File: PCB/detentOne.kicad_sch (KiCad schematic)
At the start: 0 parts

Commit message: Adding microSD
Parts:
- added U3: ESP32-S3-WROOM-1(N16R8), easyeda2kicad:WIRELM-SMD_ESP32-S3-WROOM-1, symbol easyeda2kicad:ESP32-S3-WROOM-1(N16R8)
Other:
- added sheet Encoder (Encoder.kicad_sch)
- added sheet OLED (untitled.kicad_sch)
- added sheet Switches (Switches.kicad_sch)
- added sheet TMC6300 BLDC Driver (TMC6300_BLDC.kicad_sch)
- added sheet microSD (microSD.kicad_sch)

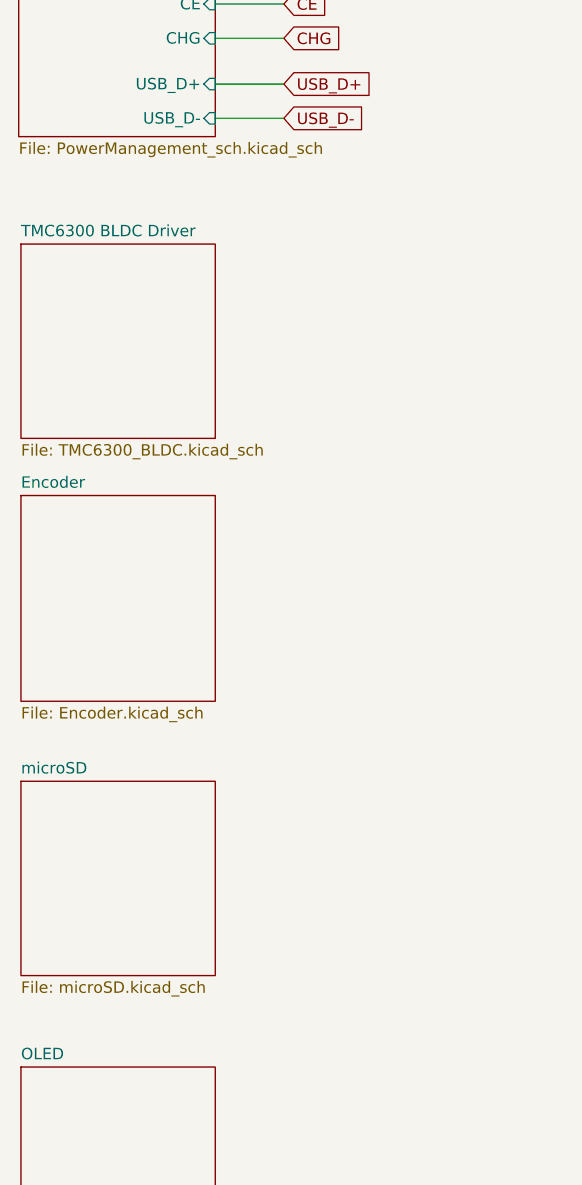
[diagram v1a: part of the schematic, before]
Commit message: Added bldc driver
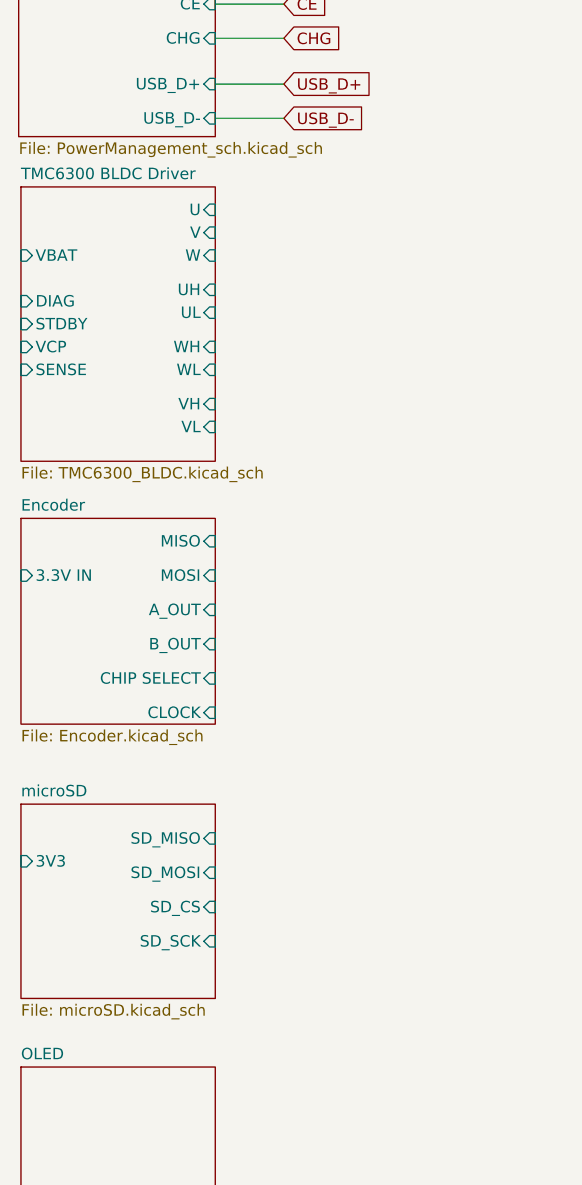
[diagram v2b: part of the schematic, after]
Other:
- sheet Encoder ports: added 3.3V IN, A_OUT, B_OUT, CHIP SELECT, CLOCK, MISO, MOSI; removed none
- sheet TMC6300 BLDC Driver ports: added DIAG, SENSE, STDBY, U, UH, UL, V, VBAT, VCP, VH, VL, W, WH, WL; removed none
- sheet microSD ports: added 3V3, SD_CS, SD_MISO, SD_MOSI, SD_SCK; removed none
- title: (none) -> detent One

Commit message: Finished schematic
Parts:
- added C16, C18: 0.1uF 6.3V, Capacitor_SMD:C_0603_1608Metric_Pad1.08x0.95mm_HandSolder, symbol Device:C
- added C17: 10uF 6.3V, Capacitor_SMD:C_0603_1608Metric_Pad1.08x0.95mm_HandSolder, symbol Device:C
- added R20, R21: 10K, Resistor_SMD:R_0603_1608Metric_Pad0.98x0.95mm_HandSolder, symbol Device:R
- added SW7, SW8: C92589, easyeda2kicad:KEY-SMD_4P-L4.2-W3.2-P2.20-LS5.1-TL, symbol Switch:SW_MEC_5E
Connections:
- net 3V3: now also U3.2 (3V3), C16.2, C17.2, R20.1, R21.2
- net CE: now also U3.39 (IO1)
- net CHG: now also U3.38 (IO2)
- net USB_D+: now also U3.14 (IO20)
- net USB_D-: now also U3.13 (IO19)
- net GND: now reaches U3.1 (GND)
- net GND: now also C16.1, C17.1, C18.2, SW7.1, SW7.2, SW8.1, SW8.2
- net A_OUT: now reaches U3.10 (IO17)
- net B_OUT: now reaches U3.11 (IO18)
- net CURRENT_SENSE: now reaches U3.12 (IO8)
- net OLED_DC: now reaches U3.17 (IO9)
- net OLED_RST: now reaches U3.18 (IO10)
- net MOSI: now reaches U3.19 (IO11)
- net SCK: now reaches U3.20 (IO12)
- net MISO: now reaches U3.21 (IO13)
- net NEOPIXEL_DIN: now reaches U3.22 (IO14)
- net ENCODER_CS: now reaches U3.23 (IO21)
- net BOOT: now reaches U3.27 (IO0)
- net BOOT: now also R21.1, SW8.3 (K), SW8.4 (A)
- net EN: now reaches U3.3 (EN)
- net EN: now also C18.1, R20.2, SW7.3 (K), SW7.4 (A)
- net SDA: now reaches U3.31 (IO38)
- net SCL: now reaches U3.32 (IO39)
- net KEY_INT: now reaches U3.33 (IO40)
- net SD_CS: now reaches U3.34 (IO41)
- net OLED_CS: now reaches U3.35 (IO42)
- net UH: now reaches U3.4 (IO4)
- net UL: now reaches U3.5 (IO5)
- net WH: now reaches U3.6 (IO6)
- net WL: now reaches U3.7 (IO7)
- net VH: now reaches U3.8 (IO15)
- net VL: now reaches U3.9 (IO16)
- no-connect marks 0 -> 10
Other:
- added sheet NeoPixels (NeoPixels.kicad_sch)
- sheet OLED ports: added 3V3, CLK, CS, DC, DIN, RST; removed none
- sheet Switches ports: added 3V3, INT, SCL, SDA; removed none
- sheet TMC6300 BLDC Driver ports: added 3V3; removed DIAG, STDBY, VCP
- note added: "BOOT BUTTON"
- note added: "RESET BUTTON & PWR ON RESET"
- moved on the sheet: U3

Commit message: PCB layout done
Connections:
- net UH: now also U3.9 (IO16); no longer U3.4 (IO4)
- net UL: now also U3.6 (IO6); no longer U3.5 (IO5)
- net VL: now also U3.4 (IO4); no longer U3.9 (IO16)
- net WH: now also U3.7 (IO7); no longer U3.6 (IO6)
- net WL: now also U3.5 (IO5); no longer U3.7 (IO7)

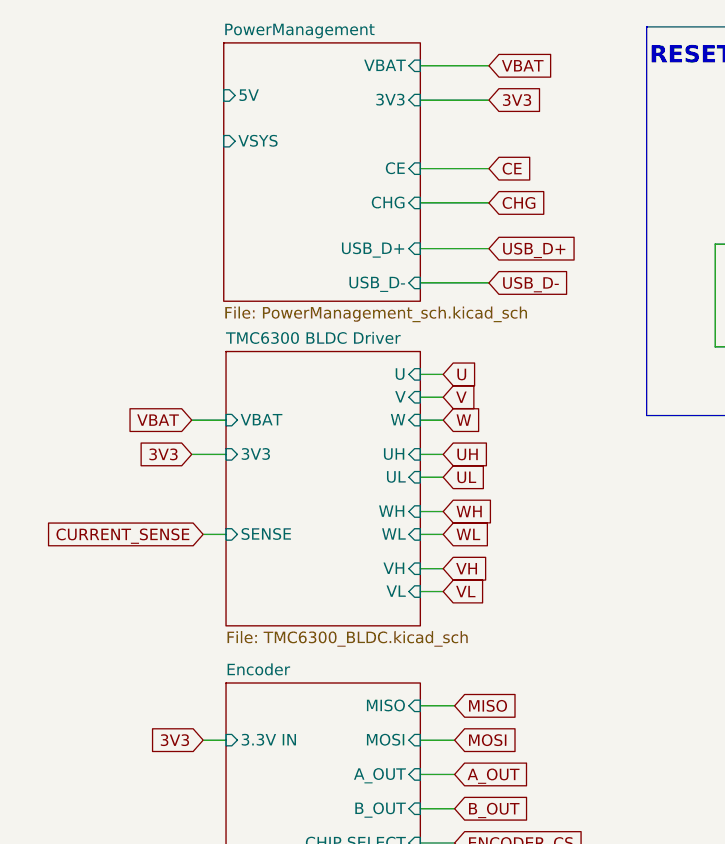
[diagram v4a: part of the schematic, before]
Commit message: PCB schematic checked - ready to trace
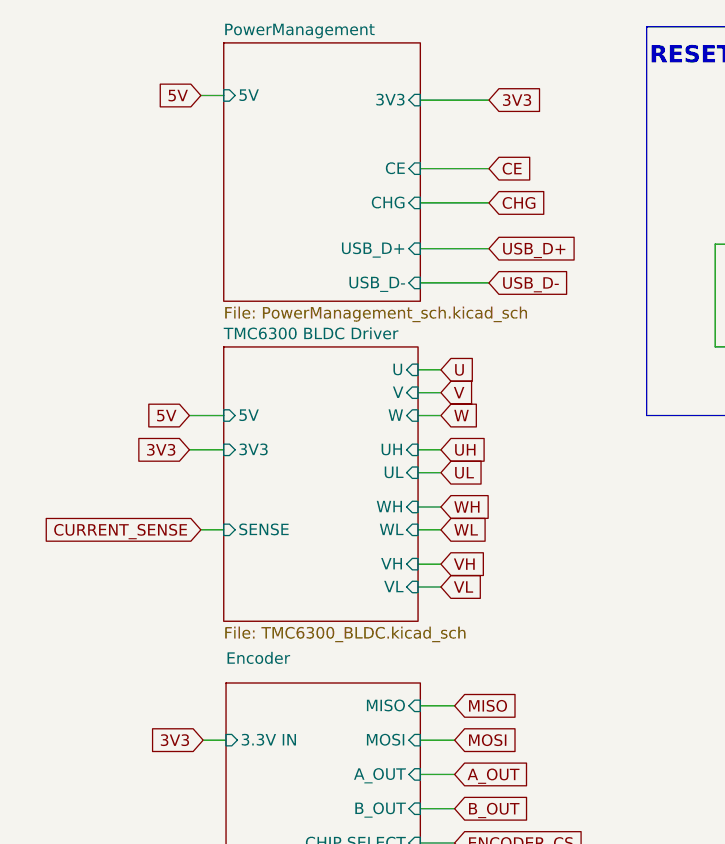
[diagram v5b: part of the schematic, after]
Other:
- sheet PowerManagement ports: added none; removed VBAT, VSYS
- sheet TMC6300 BLDC Driver ports: added 5V; removed VBAT

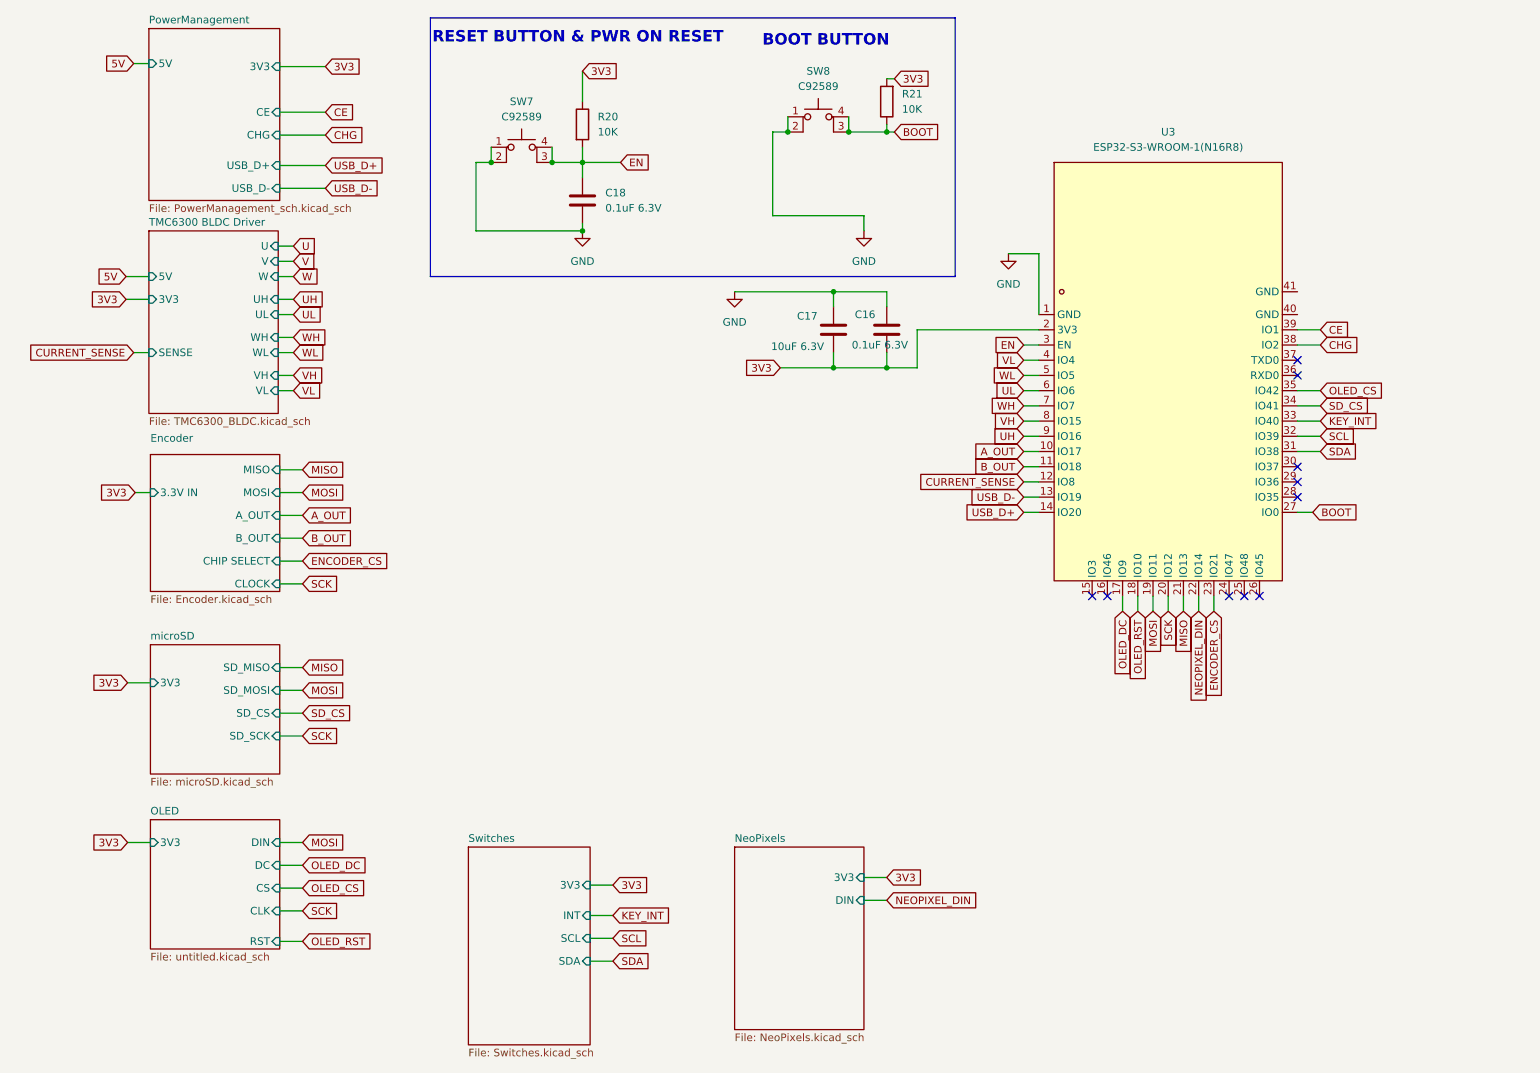
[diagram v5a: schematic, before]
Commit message: PCB tracing - encoder and SPI left
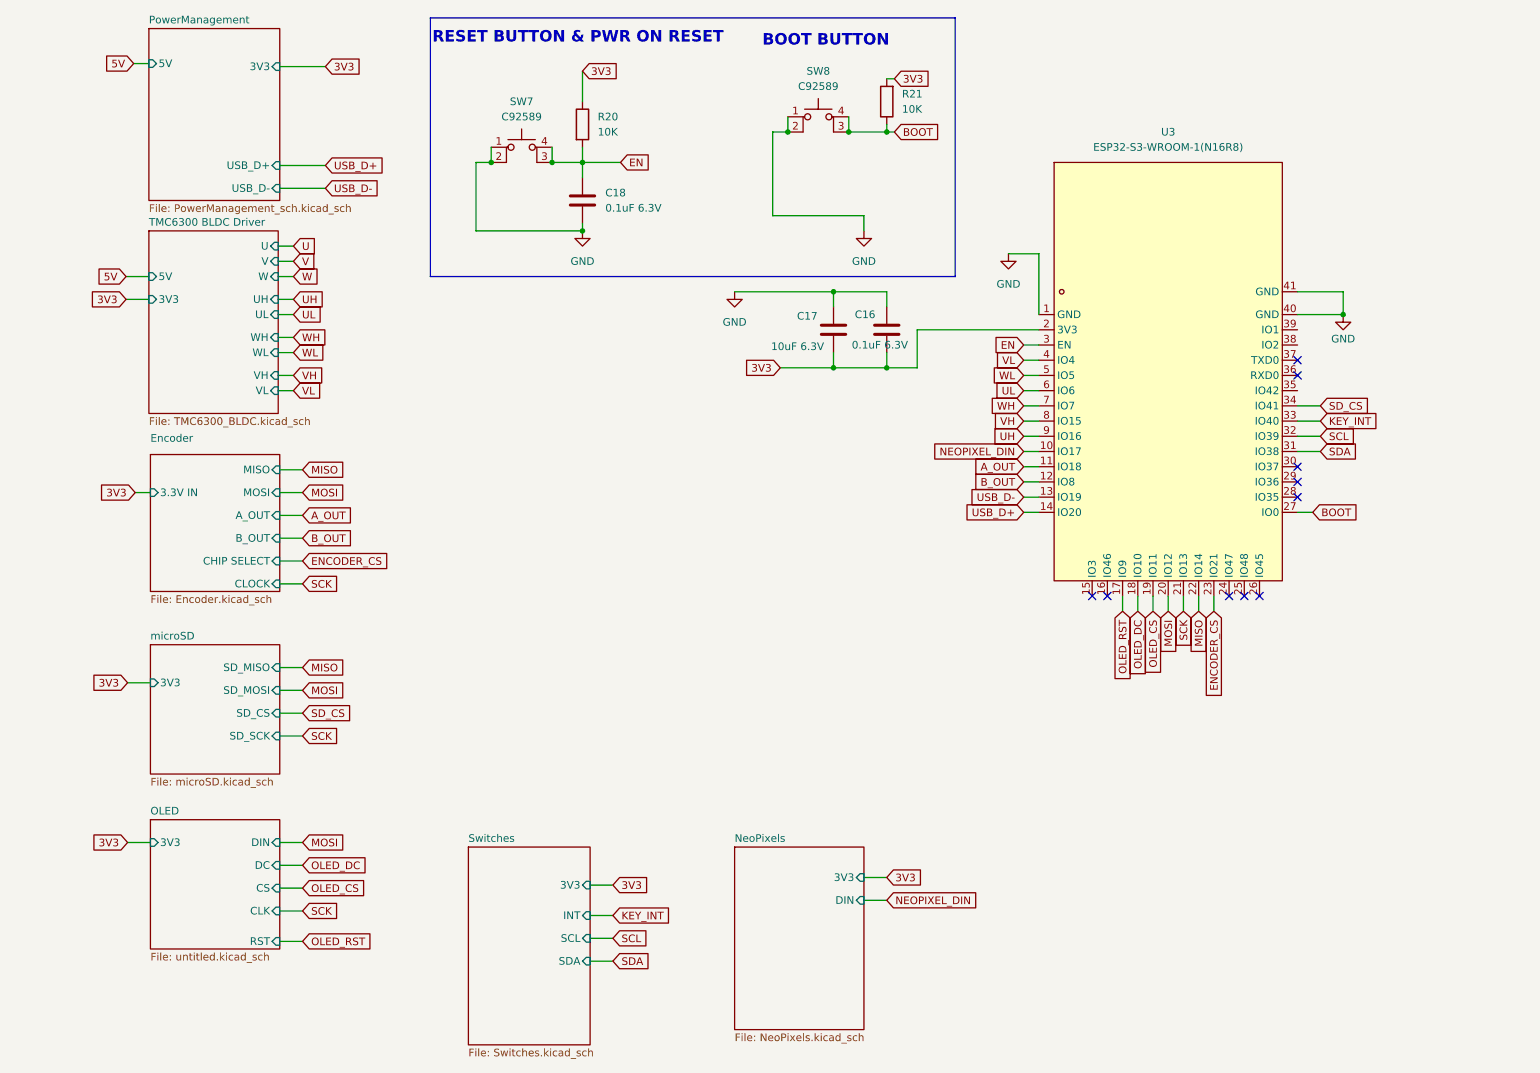
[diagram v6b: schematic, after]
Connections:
- net CURRENT_SENSE is gone; now on net B_OUT: U3.12 (IO8)
- net A_OUT: now also U3.11 (IO18); no longer U3.10 (IO17)
- net B_OUT: no longer U3.11 (IO18)
- net GND: now also U3.40 (GND), U3.41 (GND)
- net MISO: now also U3.22 (IO14); no longer U3.21 (IO13)
- net MOSI: now also U3.20 (IO12); no longer U3.19 (IO11)
- net NEOPIXEL_DIN: now also U3.10 (IO17); no longer U3.22 (IO14)
- net OLED_CS: now also U3.19 (IO11); no longer U3.35 (IO42)
- net OLED_DC: now also U3.18 (IO10); no longer U3.17 (IO9)
- net OLED_RST: now also U3.17 (IO9); no longer U3.18 (IO10)
- net SCK: now also U3.21 (IO13); no longer U3.20 (IO12)
- net CE: no longer names the net of U3.39 (IO1)
- net CHG: no longer names the net of U3.38 (IO2)
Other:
- sheet PowerManagement ports: added none; removed CE, CHG
- sheet TMC6300 BLDC Driver ports: added none; removed SENSE

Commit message: PCB traced
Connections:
- net MISO: now also U3.20 (IO12); no longer U3.22 (IO14)
- net MOSI: now also U3.22 (IO14); no longer U3.20 (IO12)
